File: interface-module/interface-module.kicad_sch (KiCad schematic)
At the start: 47 parts, among them J4 Conn_01x08, J6 Conn_01x08, SW1 SW_Coded_SH-7050, U10 TCA9548ARGER, U11 MCP3464

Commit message: Fixed footprints
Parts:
- C1, C2, C4, C5: footprint (none) -> Capacitor_SMD:C_0603_1608Metric; DPN (none) -> 1276-1861-1-ND; MPN (none) -> CL10A105KL8NNNC
- C3, C6: footprint (none) -> Capacitor_SMD:C_0603_1608Metric; DPN (none) -> 478-0603DD106MAT2ACT-ND; MPN (none) -> 0603DD106MAT2A
- C7: footprint (none) -> Capacitor_SMD:C_0603_1608Metric; DPN (none) -> 1276-1938-1-ND; MPN (none) -> CL10B104KO8NFNC
- R1, R3: footprint (none) -> Resistor_SMD:R_0603_1608Metric; DPN (none) -> RMCF0603FT10K0CT-ND; MPN (none) -> RMCF0603FT10K0
- R10, R5, R6, R7, R8: footprint (none) -> Resistor_SMD:R_0603_1608Metric; DPN (none) -> RMCF0603ZT0R00CT-ND; MPN (none) -> RMCF0603ZT0R00
- R11, R12, R13, R14, R15, R16, R17, R18, R19, R2, R20, R21, R22, R23, R24, R25, R26, R4: footprint (none) -> Resistor_SMD:R_0603_1608Metric
- R9: footprint (none) -> Resistor_SMD:R_0603_1608Metric; DPN (none) -> RMCF0603FT1R00CT-ND; MPN (none) -> RMCF0603FT1R00
- SW1: footprint (none) -> Button_Switch_THT:Nidec_Copal_SH-7010C; DPN (none) -> CT3068-ND; MPN (none) -> 220ADA16
- U1: symbol adcmod:stm32dev -> interface_module:stm32dev
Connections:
- net +3V3: no longer U1. (GND)
- net GND: no longer U1. (GND)

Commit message: routed most of board
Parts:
- added F1: 150mA Poly, Fuse:Fuse_1206_3216Metric, symbol Device:Fuse
- added F2: 350mA Poly, Fuse:Fuse_1206_3216Metric, symbol Device:Fuse
- added J2: Conn_01x02, TestPoint:TestPoint_2Pads_Pitch2.54mm_Drill0.8mm, symbol Connector_Generic:Conn_01x02
- added R27, R28: 4k7, Resistor_SMD:R_0603_1608Metric, symbol Device:R
- added RN5, RN6: 4k7, Resistor_SMD:R_Array_Convex_4x0603, symbol Device:R_Pack04_Split
- U10: value TCA9548ARGER -> TCA9548
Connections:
- net GNDP is gone; now on net GND: J6.2 (Pin_2)
- net +3V3: now also F1.1, J2.2 (Pin_2), R27.2, R28.2, RN5.1 (R1.1), RN5.2 (R2.1), RN5.3 (R3.1), RN5.4 (R4.1), RN6.1 (R1.1), RN6.2 (R2.1), RN6.3 (R3.1), RN6.4 (R4.1)
- net I2C_SCL: now also R27.1
- net I2C_SDA: now also R28.1
- net OUT0/IN0+: now also U10.1 (SD0), RN5.8 (R1.2); no longer U10.2 (SC0)
- net OUT1/IN0-: now also U10.2 (SC0), RN5.7 (R2.2); no longer U10.1 (SD0)
- net OUT2/IN1+: now also U10.3 (SD1), RN5.6 (R3.2); no longer U10.4 (SC1)
- net OUT3/IN1-: now also U10.4 (SC1), RN5.5 (R4.2); no longer U10.3 (SD1)
- net OUT4/IN2+: now also U10.5 (SD2), RN6.8 (R1.2); no longer U10.6 (SC2)
- net OUT5/IN2-: now also U10.6 (SC2), RN6.7 (R2.2); no longer U10.5 (SD2)
- net OUT6/IN3+: now also U10.7 (SD3), RN6.6 (R3.2); no longer U10.8 (SC3)
- net OUT7/IN3-: now also U10.8 (SC3), RN6.5 (R4.2); no longer U10.7 (SD3)
- net VBUS: now also F2.1; no longer J6.3 (Pin_3)
- net at SW1.1: now also U1.34 (PA5); no longer U1.36 (PA7)
- net at SW1.2: now also U1.36 (PA7); no longer U1.25 (PA8)
- net at SW1.4: now also U1.33 (PA4); no longer U1.26 (PA9)
- net at SW1.8: now also U1.35 (PA6); no longer U1.27 (PA10)
- net at U1.3 (BOOTSEL): now also J2.1 (Pin_1)
- net VPOW: no longer names the net of J6.1 (Pin_1)
- net VPOW: now also F1.2
- new net: F2.2, J6.3 (Pin_3)
- no-connect marks 23 -> 20
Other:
- note added: "Max 300mA trip"
- note added: "Sensor Power Out Max 100mA"
- note removed: "External Power"
- moved on the sheet: C1, C2, C3, C4, C5, C6, C7, D1, D2, D3, D4, D5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

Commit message: Finished copper layout
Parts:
- added R29, R30, R31, R32: R_SHUNT, Resistor_SMD:R_0603_1608Metric, symbol Device:R
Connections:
- net +3V3: no longer U1.24 (3v3), U1.44 (3v3)
- net OUT0/IN0+: now also R29.1
- net OUT1/IN0-: now also R29.2
- net OUT2/IN1+: now also R30.1
- net OUT3/IN1-: now also R30.2
- net OUT4/IN2+: now also R31.1
- net OUT5/IN2-: now also R31.2
- net OUT6/IN3+: now also R32.1
- net OUT7/IN3-: now also R32.2
- no-connect marks 20 -> 22
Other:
- note added: "For 0-3.3V: R_ADC_TOP: 0 R_ADC_BTM: NP R_ADC_POS: 1k R_ADC_NEG: 1k For 0-33V: R_ADC_TOP: 100k R_ADC_BOT: 11k R_ADC_POS: 0 R_ADC_NEG: 1k For 4-20mA: R_ADC_TOP: 0 R_ADC_BOT: 10 R_ADC_POS: 1k R_ADC_NEG: 1k For higher amps: R_ADC_TOP: 0 R_ADC_BOT: NP R_ADC_POS: 1k R_ADC_NEG: 1k R_SHUNT : shunt"
- note removed: "For 0-3.3V: R_ADC_TOP: 0 R_ADC_BTM: NP R_ADC_POS: 1k R_ADC_NEG: 1k For 0-33V: R_ADC_TOP: 100k R_ADC_BOT: 11k R_ADC_POS: 0 R_ADC_NEG: 1k For 4-20mA: R_ADC_TOP: 0 R_ADC_BOT: 10 R_ADC_POS: 1k R_ADC_NEG: 1k For higher amps: R_ADC_TOP: 0 R_ADC_BOT: shunt R_ADC_POS: 1k R_ADC_NEG: 1k"
- moved on the sheet: C2, C3, C4, C5, C6, C7, D1, D2, D3, D4, D5, D6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

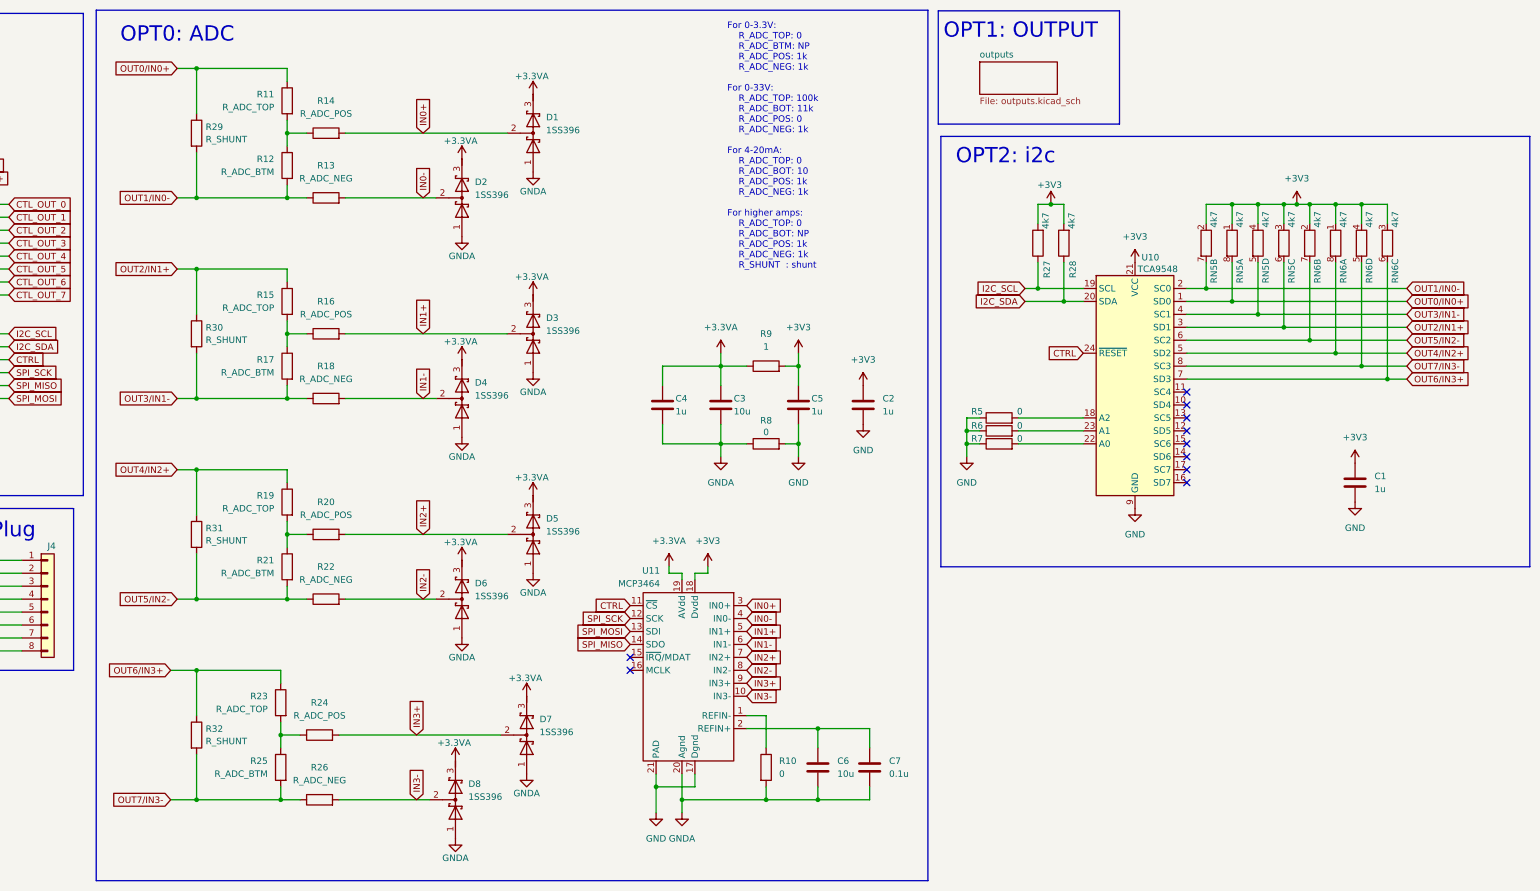
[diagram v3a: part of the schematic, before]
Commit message: Updated silkscreen
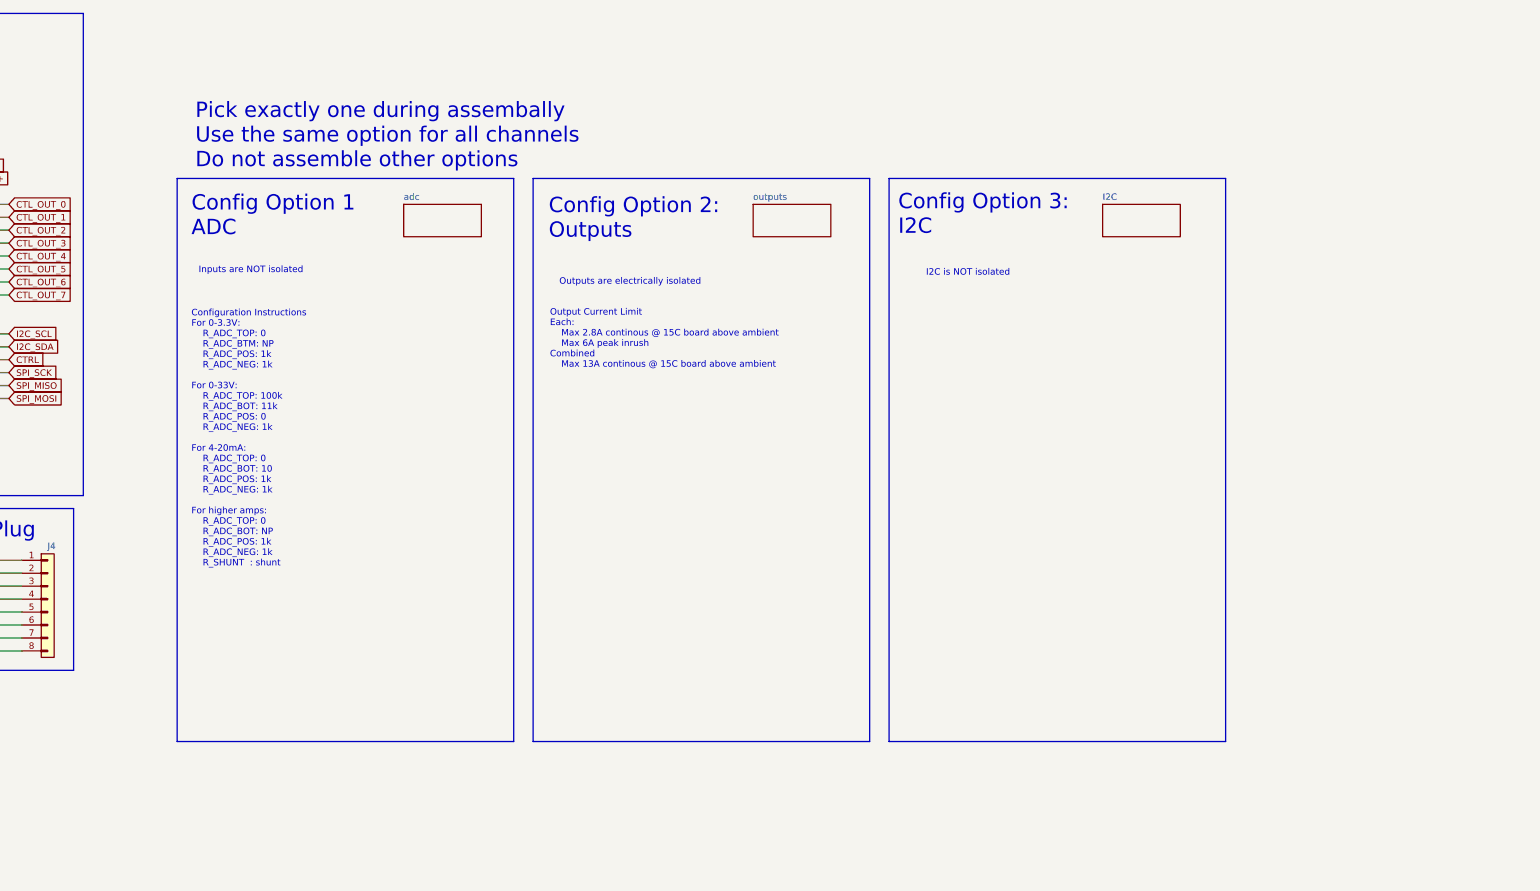
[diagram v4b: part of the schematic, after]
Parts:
- removed C1, C2, C4, C5: 1u, Capacitor_SMD:C_0603_1608Metric, symbol Device:C
- removed C3, C6: 10u, Capacitor_SMD:C_0603_1608Metric, symbol Device:C
- removed C7: 0.1u, Capacitor_SMD:C_0603_1608Metric, symbol Device:C
- removed D1, D2, D3, D4, D5, D6, D7, D8: 1SS396, Package_TO_SOT_SMD:SOT-23-3, symbol Device:D_Schottky_Dual_Series_ACK
- removed R10, R5, R6, R7, R8: 0, Resistor_SMD:R_0603_1608Metric, symbol Device:R
- removed R11, R15, R19, R23: R_ADC_TOP, Resistor_SMD:R_0603_1608Metric, symbol Device:R
- removed R12, R17, R21, R25: R_ADC_BTM, Resistor_SMD:R_0603_1608Metric, symbol Device:R
- removed R13, R18, R22, R26: R_ADC_NEG, Resistor_SMD:R_0603_1608Metric, symbol Device:R
- removed R14, R16, R20, R24: R_ADC_POS, Resistor_SMD:R_0603_1608Metric, symbol Device:R
- removed R27, R28: 4k7, Resistor_SMD:R_0603_1608Metric, symbol Device:R
- removed R29, R30, R31, R32: R_SHUNT, Resistor_SMD:R_0603_1608Metric, symbol Device:R
- removed R9: 1, Resistor_SMD:R_0603_1608Metric, symbol Device:R
- removed RN5, RN6: 4k7, Resistor_SMD:R_Array_Convex_4x0603, symbol Device:R_Pack04_Split
- removed U10: TCA9548, Package_DFN_QFN:Texas_RGE0024C_VQFN-24-1EP_4x4mm_P0.5mm_EP2.1x2.1mm, symbol Interface_Expansion:TCA9548ARGER
- removed U11: MCP3464, Package_DFN_QFN:UQFN-20-1EP_3x3mm_P0.4mm_EP1.85x1.85mm, symbol MCP3464:MCP3464
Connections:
- no-connect marks 22 -> 12
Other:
- added sheet I2C (config3_i2c.kicad_sch)
- added sheet adc (config1_adc.kicad_sch)
- sheet outputs: file outputs.kicad_sch -> config2_outputs.kicad_sch
- note added: "Config Option 1 ADC"
- note added: "Config Option 2: Outputs"
- note added: "Config Option 3: I2C"
- note added: "Configuration Instructions For 0-3.3V: R_ADC_TOP: 0 R_ADC_BTM: NP R_ADC_POS: 1k R_ADC_NEG: 1k For 0-33V: R_ADC_TOP: 100k R_ADC_BOT: 11k R_ADC_POS: 0 R_ADC_NEG: 1k For 4-20mA: R_ADC_TOP: 0 R_ADC_BOT: 10 R_ADC_POS: 1k R_ADC_NEG: 1k For higher amps: R_ADC_TOP: 0 R_ADC_BOT: NP R_ADC_POS: 1k R_ADC_NEG: 1k R_SHUNT : shunt"
- note added: "I2C is NOT isolated"
- note added: "Inputs are NOT isolated"
- note added: "Output Current Limit Each: Max 2.8A continous @ 15C board above ambient Max 6A peak inrush Combined Max 13A continous @ 15C board above ambient"
- note added: "Outputs are electrically isolated"
- note added: "Pick exactly one during assembally Use the same option for all channels Do not assemble other options"
- note removed: "For 0-3.3V: R_ADC_TOP: 0 R_ADC_BTM: NP R_ADC_POS: 1k R_ADC_NEG: 1k For 0-33V: R_ADC_TOP: 100k R_ADC_BOT: 11k R_ADC_POS: 0 R_ADC_NEG: 1k For 4-20mA: R_ADC_TOP: 0 R_ADC_BOT: 10 R_ADC_POS: 1k R_ADC_NEG: 1k For higher amps: R_ADC_TOP: 0 R_ADC_BOT: NP R_ADC_POS: 1k R_ADC_NEG: 1k R_SHUNT : shunt"
- note removed: "OPT0: ADC"
- note removed: "OPT1: OUTPUT"
- note removed: "OPT2: i2c"

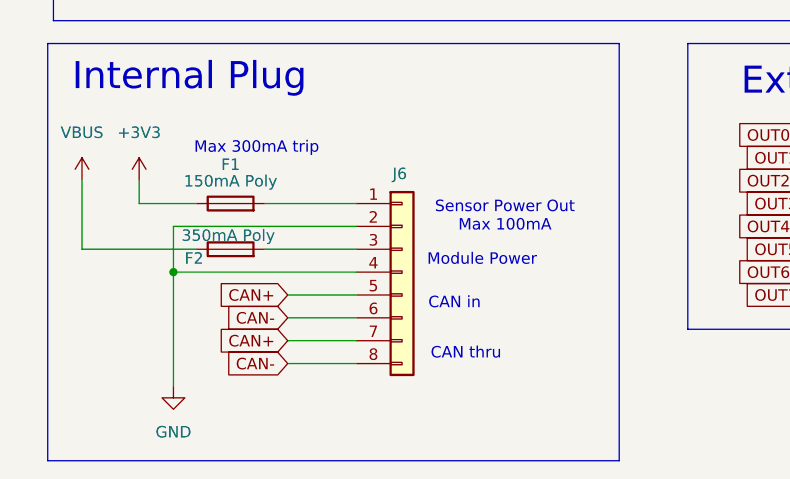
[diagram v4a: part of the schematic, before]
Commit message: More silkscreen and fixing some footprints
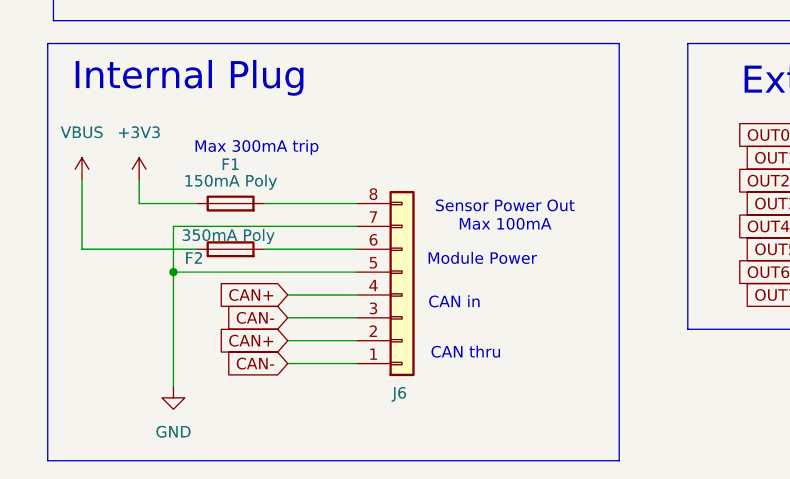
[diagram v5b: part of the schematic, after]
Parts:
- J4, J6: footprint TerminalBlock:TerminalBlock_bornier-8_P5.08mm -> footprints:TerminalBlock_CUI-8_P5.08mm
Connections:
- net CAN+: now also J6.2 (Pin_2), J6.4 (Pin_4); no longer J6.5 (Pin_5), J6.7 (Pin_7)
- net CAN-: now also J6.1 (Pin_1), J6.3 (Pin_3); no longer J6.6 (Pin_6), J6.8 (Pin_8)
- net GND: now also J6.5 (Pin_5), J6.7 (Pin_7); no longer J6.2 (Pin_2), J6.4 (Pin_4)
- net at F1.2: now also J6.8 (Pin_8); no longer J6.1 (Pin_1)
- net at F2.2: now also J6.6 (Pin_6); no longer J6.3 (Pin_3)
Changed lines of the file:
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@@
 	(symbol
 		(lib_id "Connector_Generic:Conn_01x08")
-		(at 58.42 143.51 0)
+		(at 58.42 146.05 0)
+		(mirror x)
 		(unit 1)
 		(exclude_from_sim no)
@@
 		(dnp no)
 		(property "Reference" "J6"
-			(at 58.166 132.588 0)
+			(at 58.166 156.972 0)
 			(effects
 				(font
@@
 		)
 		(property "Value" "Conn_01x08"
-			(at 58.42 130.302 0)
-			(effects
-				(font
-					(size 1.27 1.27)
-				)
-				(hide yes)
-			)
-		)
-		(property "Footprint" "TerminalBlock:TerminalBlock_bornier-8_P5.08mm"
-			(at 58.42 143.51 0)
+			(at 58.42 159.258 0)
+			(effects
+				(font
+					(size 1.27 1.27)
+				)
+				(hide yes)
+			)
+		)
+		(property "Footprint" "footprints:TerminalBlock_CUI-8_P5.08mm"
+			(at 58.42 146.05 0)
 			(effects
 				(font
@@
 		)
 		(property "Datasheet" "https://www.cuidevices.com/product/resource/tb007-508.pdf"
-			(at 58.42 143.51 0)
+			(at 58.42 146.05 0)
 			(effects
 				(font
@@
 		)
 		(property "Description" "8 Position Wire to Board Terminal Block Horizontal with Board 0.200\" (5.08mm) Through Hole"
-			(at 58.42 143.51 0)
+			(at 58.42 146.05 0)
 			(effects
 				(font
@@
 		)
 		(property "DPN" "102-6209-ND"
-			(at 58.42 143.51 0)
+			(at 58.42 146.05 0)
 			(effects
 				(font
@@
 		)
 		(property "MPN" "TB007-508-08BE"
-			(at 58.42 143.51 0)
+			(at 58.42 146.05 0)
 			(effects
 				(font
@@
 			)
 		)
-		(property "Footprint" "TerminalBlock:TerminalBlock_bornier-8_P5.08mm"
+		(property "Footprint" "footprints:TerminalBlock_CUI-8_P5.08mm"
 			(at 125.73 135.89 0)
 			(effects

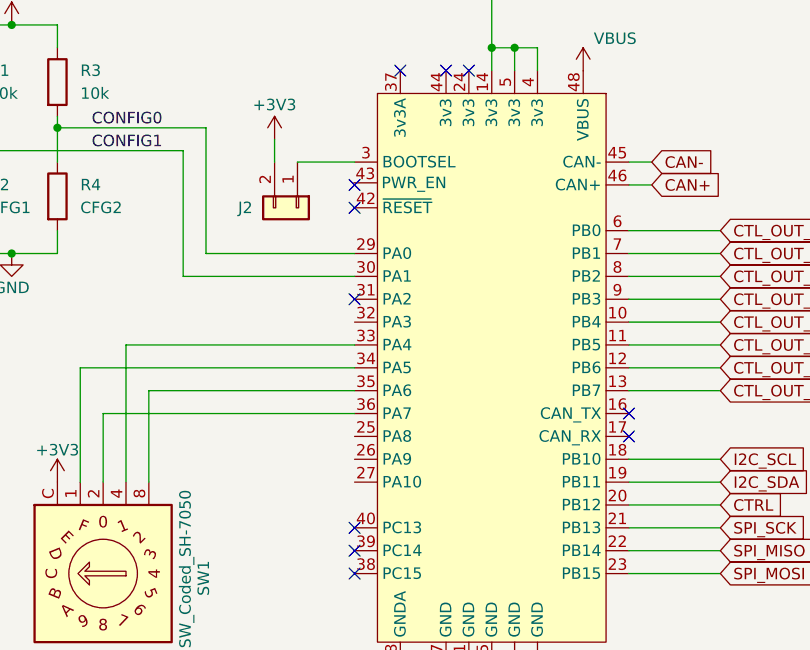
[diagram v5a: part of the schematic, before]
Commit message: Added ADC biasing resistor
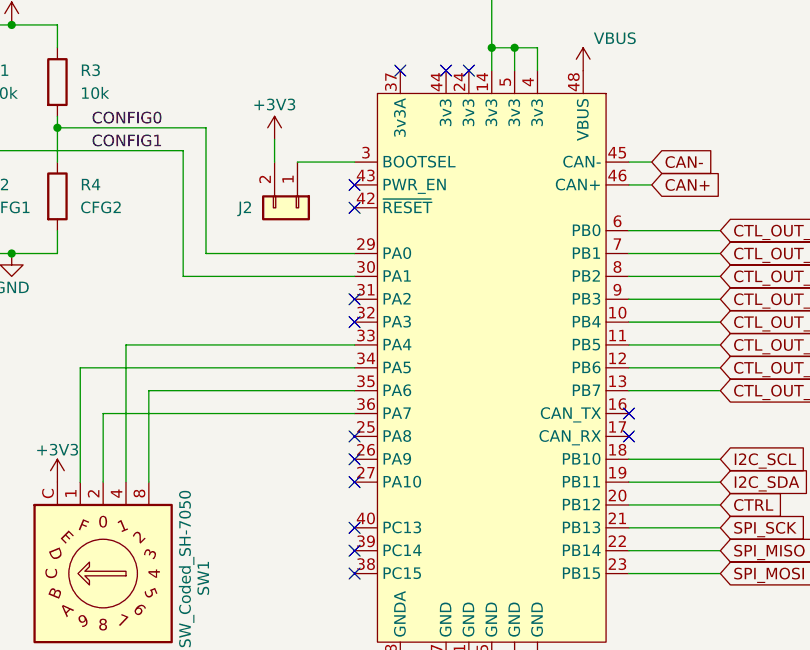
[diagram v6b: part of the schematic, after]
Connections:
- no-connect marks 12 -> 16
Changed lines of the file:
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@@
+	)
+	(no_connect
+		(at 77.47 83.82)
 	)
 	(no_connect
 		(at 77.47 66.04)
-	)
-	(no_connect
-		(at 77.47 53.34)
 	)
 	(no_connect
@@
 	)
 	(no_connect
+		(at 77.47 53.34)
+	)
+	(no_connect
+		(at 77.47 86.36)
+	)
+	(no_connect
 		(at 77.47 55.88)
 	)
@@
 	)
 	(no_connect
+		(at 77.47 68.58)
+	)
+	(no_connect
 		(at 107.95 78.74)
 	)
 	(no_connect
+		(at 77.47 81.28)
+	)
+	(no_connect
